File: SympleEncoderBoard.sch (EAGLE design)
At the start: 1 part

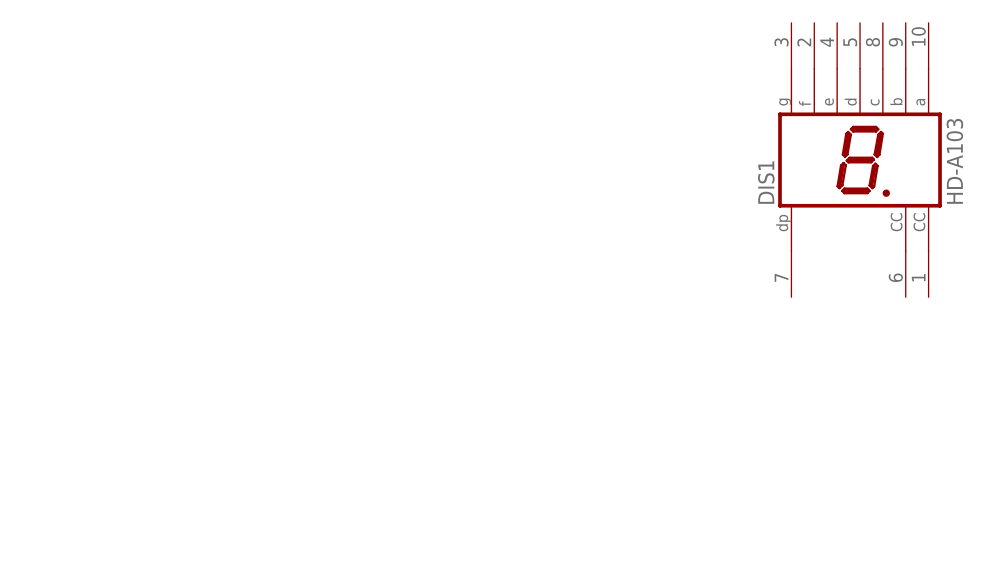
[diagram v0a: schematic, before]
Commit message: .schと.brd作ったよ
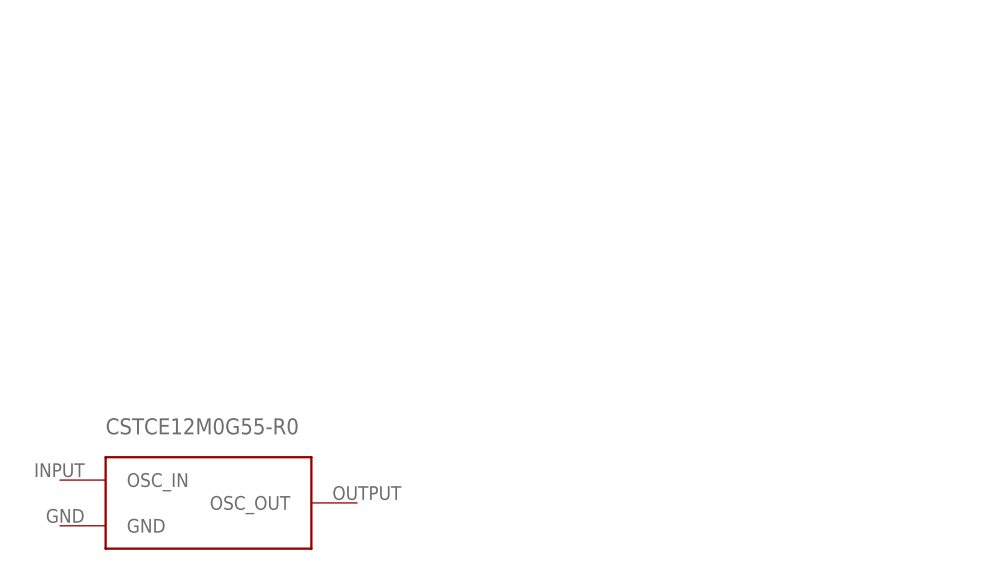
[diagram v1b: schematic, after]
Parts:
- removed DIS1: HD-A103, display-hp:HD-A103
- added Y1: CSTCE12M0G55-_R0, SympleEncoderBoard:CSTCE12M0G55-_R0
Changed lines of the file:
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@@
 </classes>
 <parts>
-<part name="DIS1" library="display-hp" library_urn="urn:adsk.eagle:library:212" deviceset="HD-A103" device="" package3d_urn="urn:adsk.eagle:package:12999/1"/>
+<part name="Y1" library="SympleEncoderBoard" deviceset="CSTCE12M0G55-_R0" device=""/>
 </parts>
 <sheets>
@@
 </plain>
 <instances>
-<instance part="DIS1" gate="A" x="132.08" y="93.98" smashed="yes">
-<attribute name="NAME" x="122.555" y="88.9" size="1.778" layer="95" rot="R90"/>
-<attribute name="VALUE" x="143.51" y="88.9" size="1.778" layer="96" rot="R90"/>
-</instance>
+<instance part="Y1" gate="G$1" x="55.88" y="55.88" smashed="yes"/>
 </instances>
 <busses>
@@
 </schematic>
 </drawing>
-<compatibility>
-<note version="8.2" severity="warning">
-Since Version 8.2, EAGLE supports online libraries. The ids
-of those online libraries will not be understood (or retained)
-with this version.
-</note>
-<note version="8.3" severity="warning">
-Since Version 8.3, EAGLE supports URNs for individual library
-assets (packages, symbols, and devices). The URNs of those assets
-will not be understood (or retained) with this version.
-</note>
-<note version="8.3" severity="warning">
-Since Version 8.3, EAGLE supports the association of 3D packages
-with devices in libraries, schematics, and board files. Those 3D
-packages will not be understood (or retained) with this version.
-</note>
-</compatibility>
 </eagle>

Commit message: ライブラリとかバスを作っただけ
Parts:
- removed Y1: CSTCE12M0G55-_R0, SympleEncoderBoard:CSTCE12M0G55-_R0
- added IC1: STM32F446RET6, STM32F446RET6:STM32F446RET6
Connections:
- new net VCP_RX: IC1.PA3
- new net VCP_TX: IC1.PA2
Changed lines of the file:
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@@
 <setting verticaltext="up"/>
 </settings>
-<grid distance="0.1" unitdist="inch" unit="inch" style="lines" multiple="1" display="no" altdistance="0.01" altunitdist="inch" altunit="inch"/>
+<grid distance="1" unitdist="mm" unit="mm" style="lines" multiple="1" display="yes" altdistance="0.25" altunitdist="mm" altunit="mm"/>
 <layers>
 <layer number="1" name="Top" color="4" fill="1" visible="no" active="no"/>
@@
 </classes>
 <parts>
-<part name="Y1" library="SympleEncoderBoard" deviceset="CSTCE12M0G55-_R0" device=""/>
+<part name="IC1" library="STM32F446RET6" deviceset="STM32F446RET6" device=""/>
 </parts>
 <sheets>
@@
 </plain>
 <instances>
-<instance part="Y1" gate="G$1" x="55.88" y="55.88" smashed="yes"/>
+<instance part="IC1" gate="G$1" x="86.36" y="71.12" smashed="yes">
+<attribute name="NAME" x="135.89" y="88.9" size="1.778" layer="95" align="center-left"/>
+<attribute name="VALUE" x="135.89" y="86.36" size="1.778" layer="96" align="center-left"/>
+</instance>
 </instances>
 <busses>
+<bus name="+3.3V,GND,NRST,SWCLK,SWDIO,SWO,VCP_RX,VCP_TX">
+<segment>
+<wire x1="79" y1="9" x2="79" y2="95" width="0.762" layer="92"/>
+<wire x1="79" y1="95" x2="160" y2="95" width="0.762" layer="92"/>
+<wire x1="160" y1="95" x2="160" y2="25" width="0.762" layer="92"/>
+</segment>
+</bus>
+<bus name="+3.3V,+5V,CAN_RX,CAN_TX,EN1_A,EN1_B,EN2_A,EN2_B,EN3_A,EN3_B,EN4_A,EN4_B,ENX_A,ENX_B,ENY_A,ENY_B,ERRORLED,GND,I2C_SCL,I2C_SDA,LED1,LED2,LEDGYRO,OSC_IN,OSC_OUT,SW1,SW2,SW3,SW4,SW5,SW6,SW7,SW8,SW9">
+<segment>
+<wire x1="173" y1="6" x2="88" y2="6" width="0.762" layer="92"/>
+<wire x1="173" y1="6" x2="173" y2="106" width="0.762" layer="92"/>
+<wire x1="173" y1="106" x2="64" y2="106" width="0.762" layer="92"/>
+<wire x1="64" y1="106" x2="64" y2="27" width="0.762" layer="92"/>
+</segment>
+</bus>
 </busses>
 <nets>
+<net name="VCP_RX" class="0">
+<segment>
+<pinref part="IC1" gate="G$1" pin="PA3"/>
+<wire x1="93.98" y1="15.24" x2="79" y2="15.24" width="0.1524" layer="91"/>
+<wire x1="79" y1="15.24" x2="79" y2="16" width="0.1524" layer="91"/>
+</segment>
+</net>
+<net name="VCP_TX" class="0">
+<segment>
+<pinref part="IC1" gate="G$1" pin="PA2"/>
+<wire x1="86.36" y1="33.02" x2="86.36" y2="33" width="0.1524" layer="91"/>
+<wire x1="86.36" y1="33" x2="79" y2="33" width="0.1524" layer="91"/>
+</segment>
+</net>
 </nets>
 </sheet>

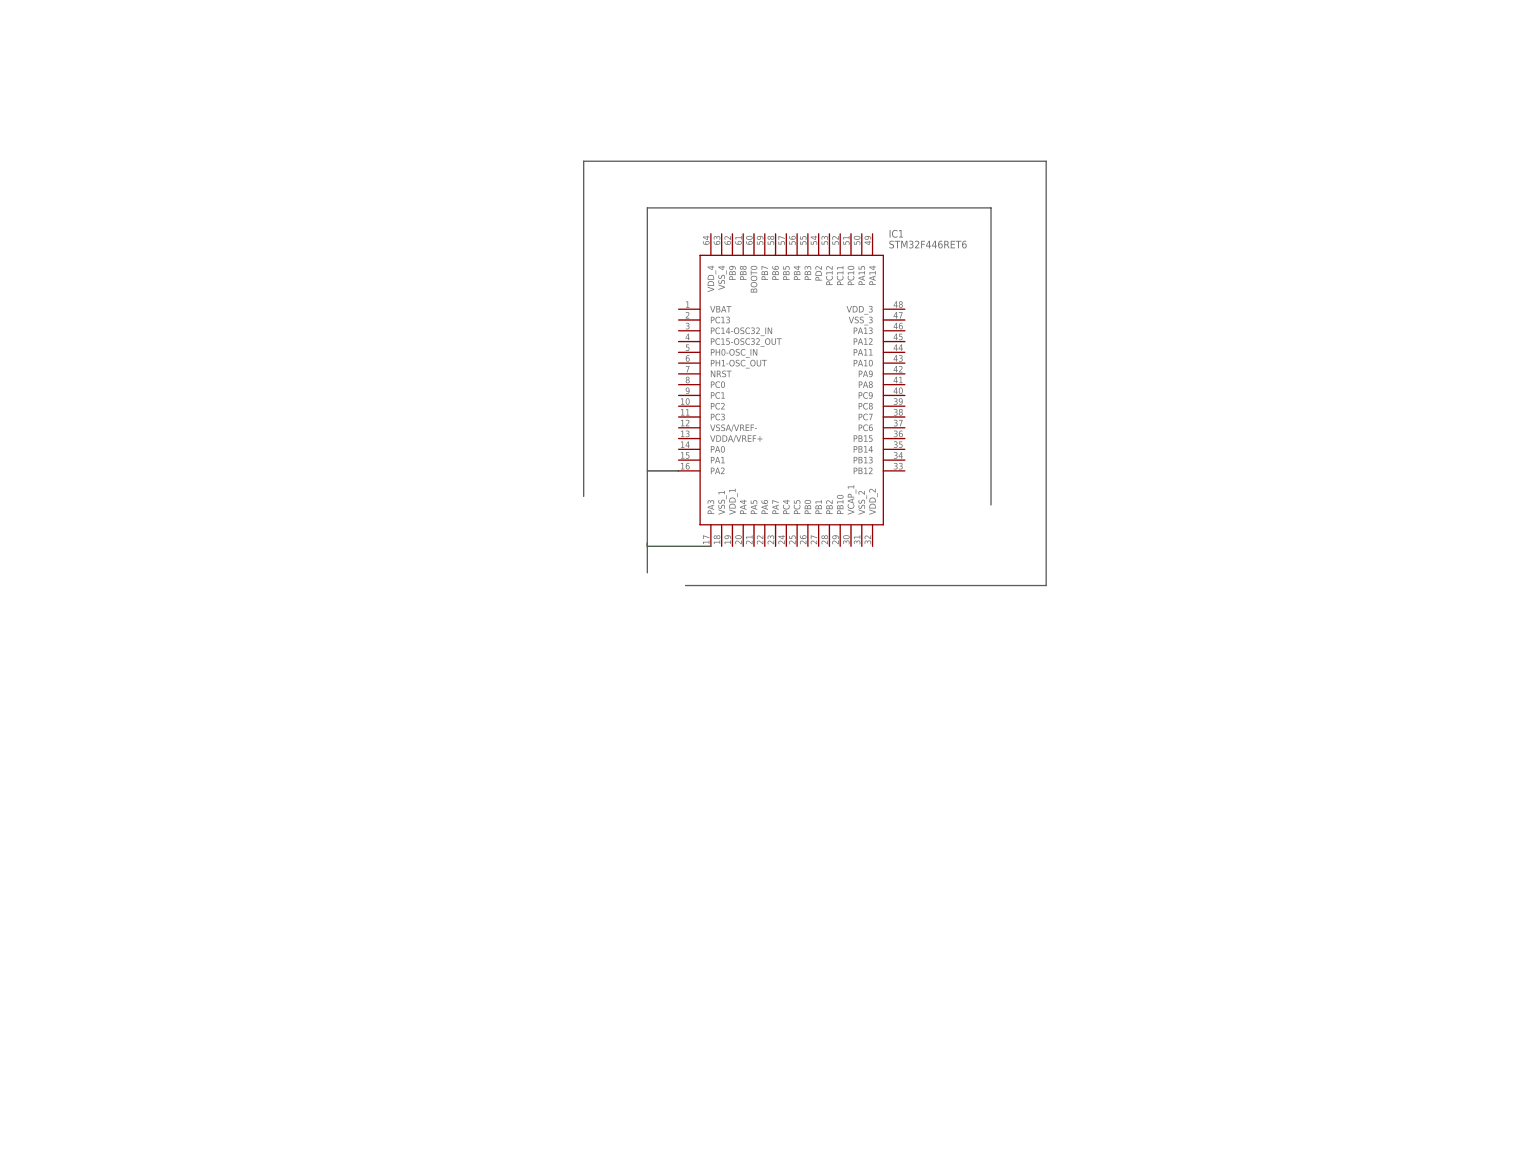
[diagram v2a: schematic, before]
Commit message: 回路図は完成、コネクタつけた
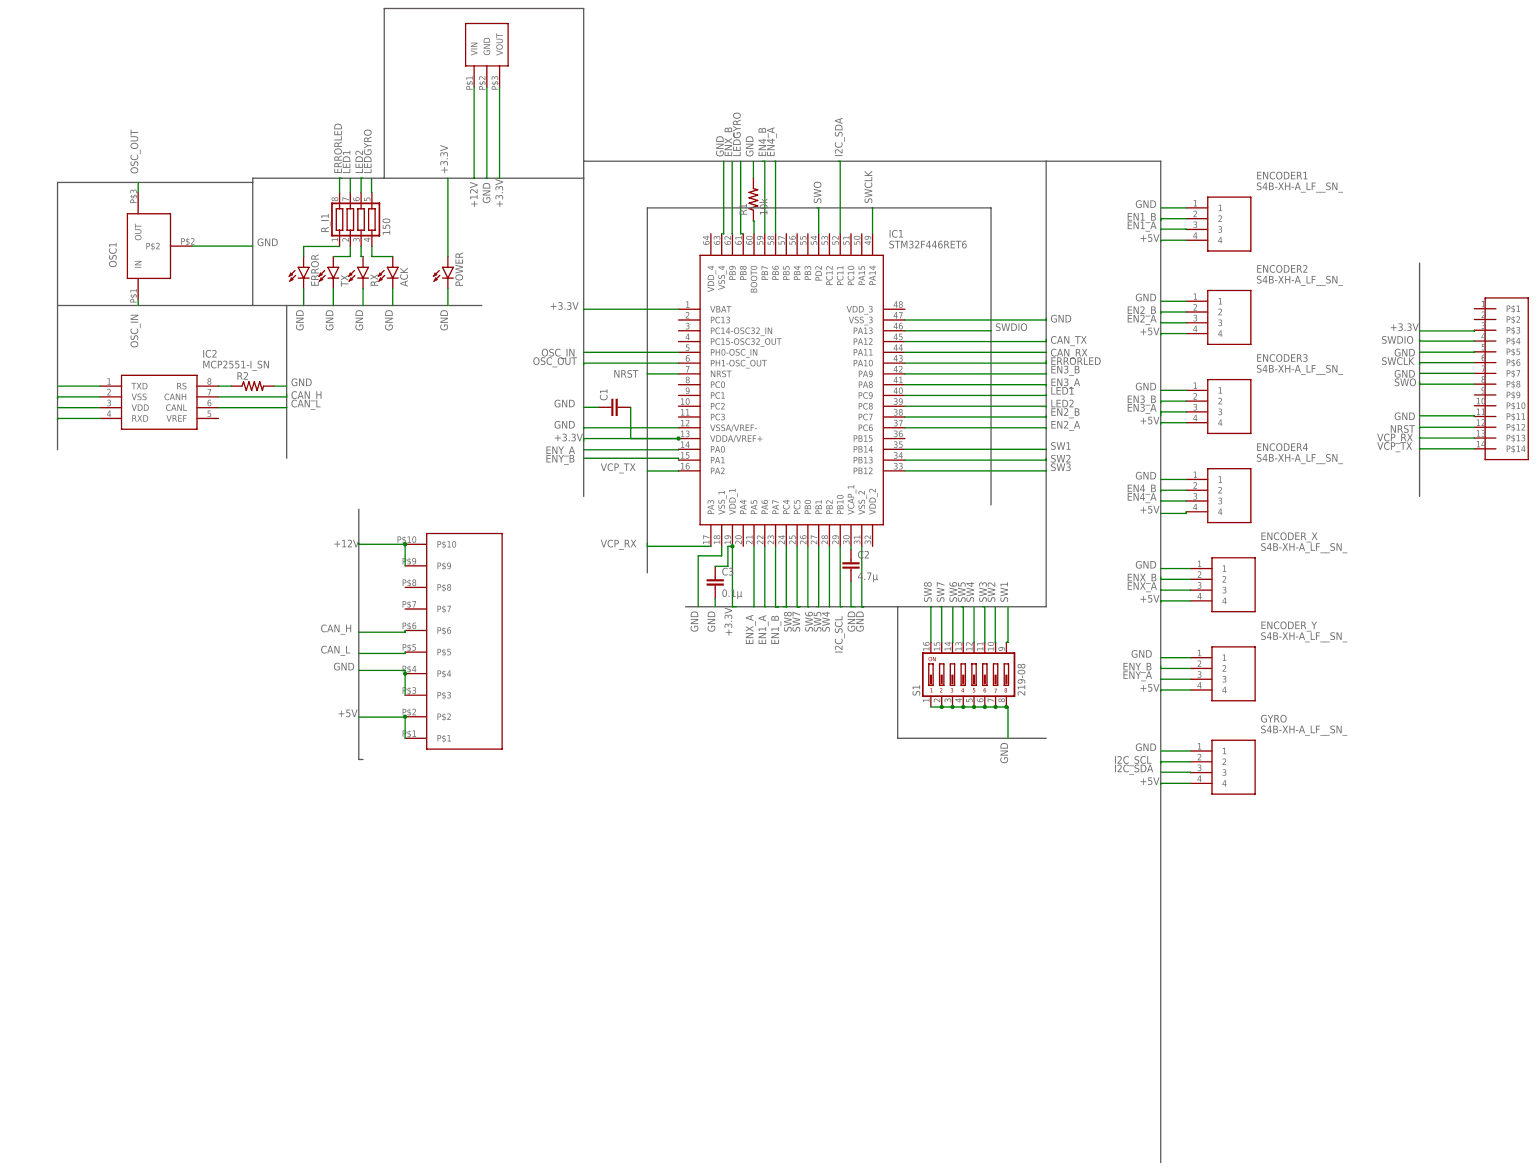
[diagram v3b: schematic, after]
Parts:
- added ACK, ERROR, POWER, RX, TX: (no value), led:LEDCHIPLED_0603
- added BOX10P-L1: BOX10PBOX10P-L, user_conector:BOX10PBOX10P-L
- added C1: (no value), rcl:C-EUC1608
- added C2: 4.7μ, rcl:C-EUC0603
- added C3: 0.1μ, rcl:C-EUC0603
- added ENCODER1, ENCODER2, ENCODER3, ENCODER4, ENCODER_X, ENCODER_Y, GYRO: S4B-XH-A_LF__SN_, S4B-XH-A_LF__SN_:S4B-XH-A_LF__SN_
- added IC2: MCP2551-I_SN, MCP2551-I_SN:MCP2551-I_SN
- added OSC1: (no value), user_osc:CSTN#
- added R1: 10k, rcl:R-US_R0603
- added R2: (no value), rcl:R-US_R0603
- added R_I1: 150, user_rcl:R_SHUGOU
- added S1: 219-08, switch-dil:219-08
- added U$1: BOX14P, user_conector:BOX14P
- added U$2: BP5293-33, SympleEncoderBoard:BP5293-33
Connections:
- new net +12V: BOX10P-L1.P$10, BOX10P-L1.P$9, U$2.VIN
- new net +3.3V: C1.2, C3.1, IC1.VBAT, IC1.VDDA/VREF+, IC1.VDD_1, POWER.A, U$1.P$3, U$2.VOUT
- new net +5V: BOX10P-L1.P$1, BOX10P-L1.P$2, ENCODER1.4, ENCODER2.4, ENCODER3.4, ENCODER4.4, ENCODER_X.4, ENCODER_Y.4, GYRO.4, IC2.VDD
- new net CAN_H: BOX10P-L1.P$6, IC2.CANH
- new net CAN_L: BOX10P-L1.P$5, IC2.CANL
- new net CAN_RX: IC1.PA11, IC2.RXD
- new net CAN_TX: IC1.PA12, IC2.TXD
- new net EN1_A: ENCODER1.3, IC1.PA6
- new net EN1_B: ENCODER1.2, IC1.PA7
- new net EN2_A: ENCODER2.3, IC1.PC6
- new net EN2_B: ENCODER2.2, IC1.PC7
- new net EN3_A: ENCODER3.3, IC1.PA8
- new net EN3_B: ENCODER3.2, IC1.PA9
- new net EN4_A: ENCODER4.3, IC1.PB6
- new net EN4_B: ENCODER4.2, IC1.PB7
- new net ENX_A: ENCODER_X.3, IC1.PA5
- new net ENX_B: ENCODER_X.2, IC1.PB9
- new net ENY_A: ENCODER_Y.3, IC1.PA0
- new net ENY_B: ENCODER_Y.2, IC1.PA1
- new net ERRORLED: IC1.PA10, R_I1.8
- new net GND: ACK.C, BOX10P-L1.P$3, BOX10P-L1.P$4, C1.1, C2.2, C3.2, ENCODER1.1, ENCODER2.1, ENCODER3.1, ENCODER4.1, ENCODER_X.1, ENCODER_Y.1, ERROR.C, GYRO.1, IC1.VSSA/VREF-, IC1.VSS_1, IC1.VSS_2, IC1.VSS_3, IC1.VSS_4, IC2.VSS, OSC1.P$2, POWER.C, R1.2, R2.2, RX.C, S1.1, S1.2, S1.3, S1.4, S1.5, S1.6, S1.7, S1.8, TX.C, U$1.P$11, U$1.P$5, U$1.P$7, U$2.GND
- new net I2C_SCL: GYRO.2, IC1.PB10
- new net I2C_SDA: GYRO.3, IC1.PC11
- new net LED1: IC1.PC9, R_I1.7
- new net LED2: IC1.PC8, R_I1.6
- new net LEDGYRO: IC1.PB8, R_I1.5
- new net N$1: IC1.BOOT0, R1.1
- new net N$2: C2.1, IC1.VCAP_1
- new net N$3: ERROR.A, R_I1.1
- new net N$4: R_I1.2, TX.A
- new net N$5: RX.A, R_I1.3
- new net N$6: ACK.A, R_I1.4
- new net N$7: IC2.RS, R2.1
- new net NRST: IC1.NRST, U$1.P$12
- new net OSC_IN: IC1.PH0-OSC_IN, OSC1.IN
- new net OSC_OUT: IC1.PH1-OSC_OUT, OSC1.OUT
- new net SW1: IC1.PB14, S1.9
- new net SW2: IC1.PB13, S1.10
- new net SW3: IC1.PB12, S1.11
- new net SW4: IC1.PB2, S1.12
- new net SW5: IC1.PB1, S1.13
- new net SW6: IC1.PB0, S1.14
- new net SW7: IC1.PC5, S1.15
- new net SW8: IC1.PC4, S1.16
- new net SWCLK: IC1.PA14, U$1.P$6
- new net SWDIO: IC1.PA13, U$1.P$4
- new net SWO: IC1.PD2, U$1.P$8
- net VCP_RX: now also U$1.P$13
- net VCP_TX: now also U$1.P$14

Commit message: 回路図書きました
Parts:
- added R3: 150, rcl:R-US_R0603
- R2: value (none) -> 33k
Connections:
- new net N$8: POWER.A, R3.1
- net +3.3V: now also R3.2; no longer POWER.A
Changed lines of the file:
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@@
 <part name="IC2" library="MCP2551-I_SN" deviceset="MCP2551-I_SN" device=""/>
 <part name="BOX10P-L1" library="user_conector" deviceset="BOX10P" device="BOX10P-L"/>
-<part name="R2" library="rcl" library_urn="urn:adsk.eagle:library:334" deviceset="R-US_" device="R0603" package3d_urn="urn:adsk.eagle:package:23555/3"/>
+<part name="R2" library="rcl" library_urn="urn:adsk.eagle:library:334" deviceset="R-US_" device="R0603" package3d_urn="urn:adsk.eagle:package:23555/3" value="33k"/>
 <part name="U$2" library="SympleEncoderBoard" deviceset="BP5293-33" device=""/>
+<part name="R3" library="rcl" library_urn="urn:adsk.eagle:library:334" deviceset="R-US_" device="R0603" package3d_urn="urn:adsk.eagle:package:23555/3" value="150"/>
 </parts>
 <sheets>
@@
 </instance>
 <instance part="U$2" gate="G$1" x="41.18" y="133.46" smashed="yes"/>
+<instance part="R3" gate="G$1" x="32" y="93" smashed="yes" rot="R90">
+<attribute name="NAME" x="30.5014" y="89.19" size="1.778" layer="95" rot="R90"/>
+<attribute name="VALUE" x="35.302" y="89.19" size="1.778" layer="96" rot="R90"/>
+</instance>
 </instances>
 <busses>
@@
 </segment>
 <segment>
-<pinref part="POWER" gate="G$1" pin="A"/>
-<wire x1="32" y1="83.54" x2="32" y2="102" width="0.1524" layer="91"/>
-<label x="32" y="103" size="1.778" layer="95" rot="R90"/>
-</segment>
-<segment>
 <pinref part="U$2" gate="G$1" pin="VOUT"/>
 <wire x1="44.18" y1="123.46" x2="44.18" y2="102" width="0.1524" layer="91"/>
 <wire x1="44.18" y1="102" x2="44" y2="102" width="0.1524" layer="91"/>
 <label x="45" y="95" size="1.778" layer="95" rot="R90"/>
+</segment>
+<segment>
+<pinref part="R3" gate="G$1" pin="2"/>
+<wire x1="32" y1="98.08" x2="32" y2="102" width="0.1524" layer="91"/>
+<label x="32" y="103" size="1.778" layer="95" rot="R90"/>
 </segment>
 </net>
@@
 <wire x1="-50" y1="50.46" x2="-60" y2="50.46" width="0.1524" layer="91"/>
 <wire x1="-60" y1="50.46" x2="-60" y2="50" width="0.1524" layer="91"/>
+<label x="-61" y="51" size="1.778" layer="95" rot="R180"/>
 </segment>
 <segment>
@@
 <pinref part="IC2" gate="G$1" pin="TXD"/>
 <wire x1="-50" y1="53" x2="-60" y2="53" width="0.1524" layer="91"/>
+<label x="-61" y="54" size="1.778" layer="95" rot="R180"/>
 </segment>
 </net>
@@
 <wire x1="-50" y1="45.38" x2="-60" y2="45.38" width="0.1524" layer="91"/>
 <wire x1="-60" y1="45.38" x2="-60" y2="45" width="0.1524" layer="91"/>
+<label x="-61" y="46" size="1.778" layer="95" rot="R180"/>
 </segment>
 </net>
@@
 <wire x1="-50" y1="47.92" x2="-60" y2="47.92" width="0.1524" layer="91"/>
 <wire x1="-60" y1="47.92" x2="-60" y2="48" width="0.1524" layer="91"/>
+<label x="-61" y="48" size="1.778" layer="95" rot="R180"/>
 </segment>
 <segment>
@@
 </segment>
 </net>
+<net name="N$8" class="0">
+<segment>
+<pinref part="R3" gate="G$1" pin="1"/>
+<pinref part="POWER" gate="G$1" pin="A"/>
+<wire x1="32" y1="87.92" x2="32" y2="83.54" width="0.1524" layer="91"/>
+</segment>
+</net>
